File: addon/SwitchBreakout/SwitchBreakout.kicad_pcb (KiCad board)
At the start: 2 copper layers, 127.8 x 194.6 mm, 207 parts, among them IC1 SN74HCS72QPWRQ1, IC10 SN74HCS72QPWRQ1, IC11 SN74HCS72QPWRQ1, IC12 SN74HCS72QPWRQ1, IC13 SN74HCS72QPWRQ1, IC14 SN74HCS72QPWRQ1, IC15 SN74HCS72QPWRQ1, IC16 SN74HCS72QPWRQ1, IC2 SN74HCS72QPWRQ1, IC3 SN74HCS72QPWRQ1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

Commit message: Via whatever
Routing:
- net /C8: track 40.9 -> 205.5 mm, vias 0 -> 2
- net /C6: track 104.6 -> 214.5 mm, vias 0 -> 2
- net /C5: track 84.2 -> 188.3 mm, vias 0 -> 2
- net /C2: track 92.2 -> 171.2 mm, vias 0 -> 2
- net /C1: track 80.8 -> 159.6 mm, vias 0 -> 2
- net /C4: track 96.9 -> 175.3 mm, vias 0 -> 2
- net Net-(F11-Pad2): track 0.00 -> 4.93 mm
- net Net-(F15-Pad2): track 0.00 -> 4.93 mm
- net /D1: track 181.5 -> 184.0 mm
- net /D2: track 186.3 -> 188.1 mm
- net /D-Latch 1-8/BTN4: track 61.9 -> 62.5 mm

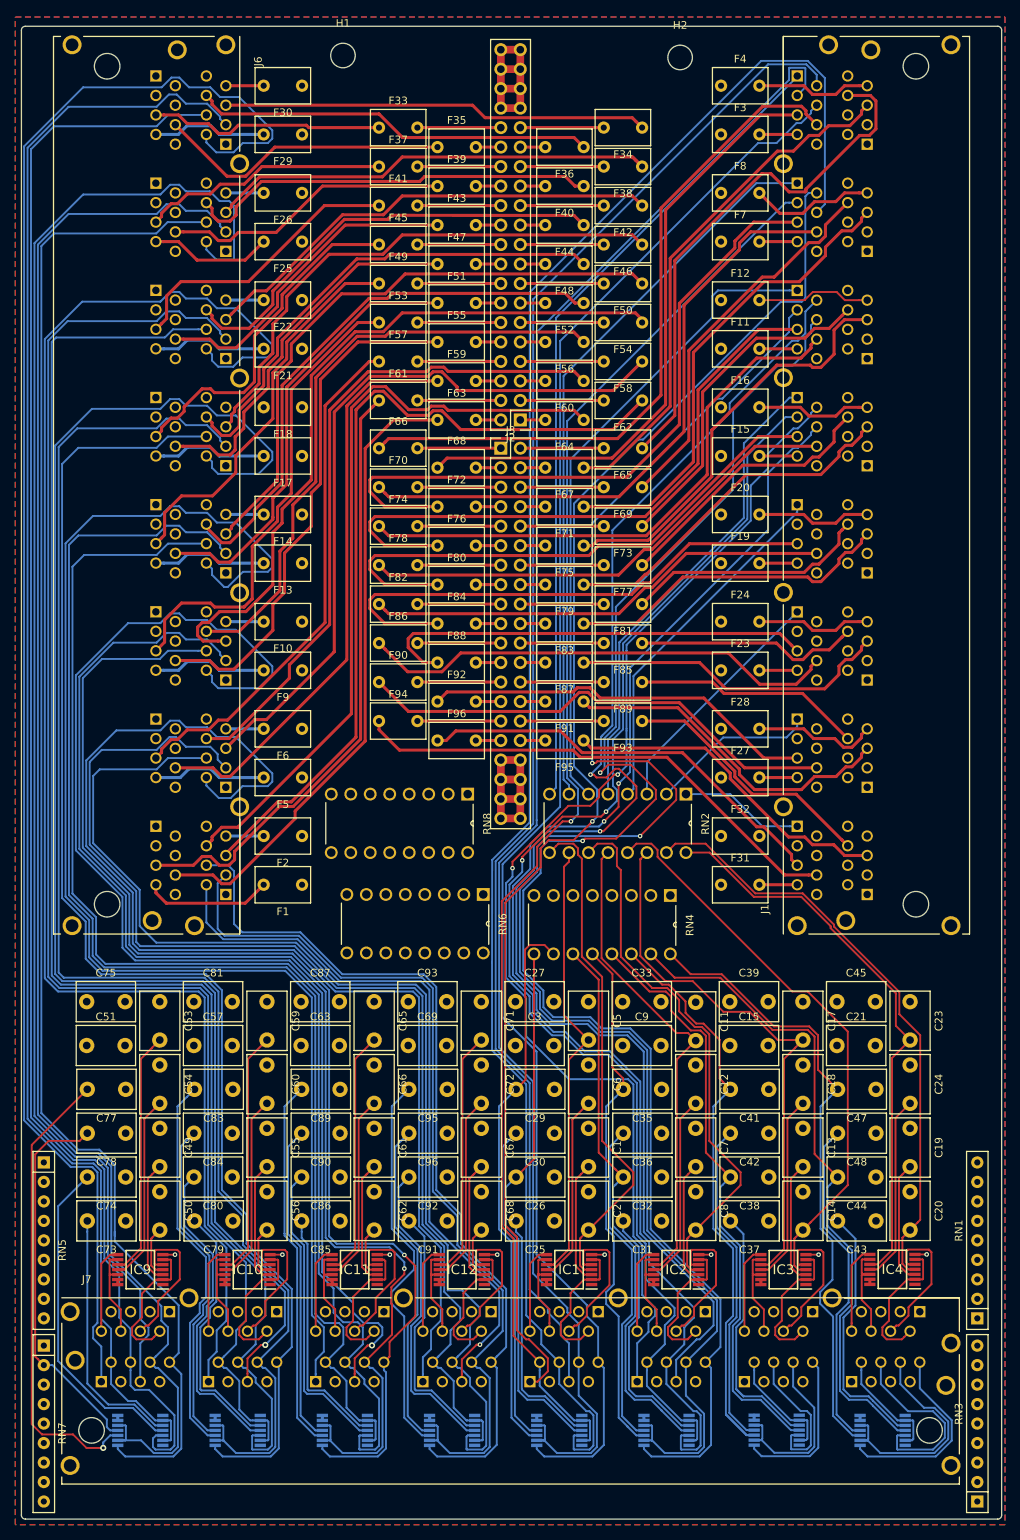
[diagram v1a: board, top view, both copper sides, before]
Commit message: Short stubs
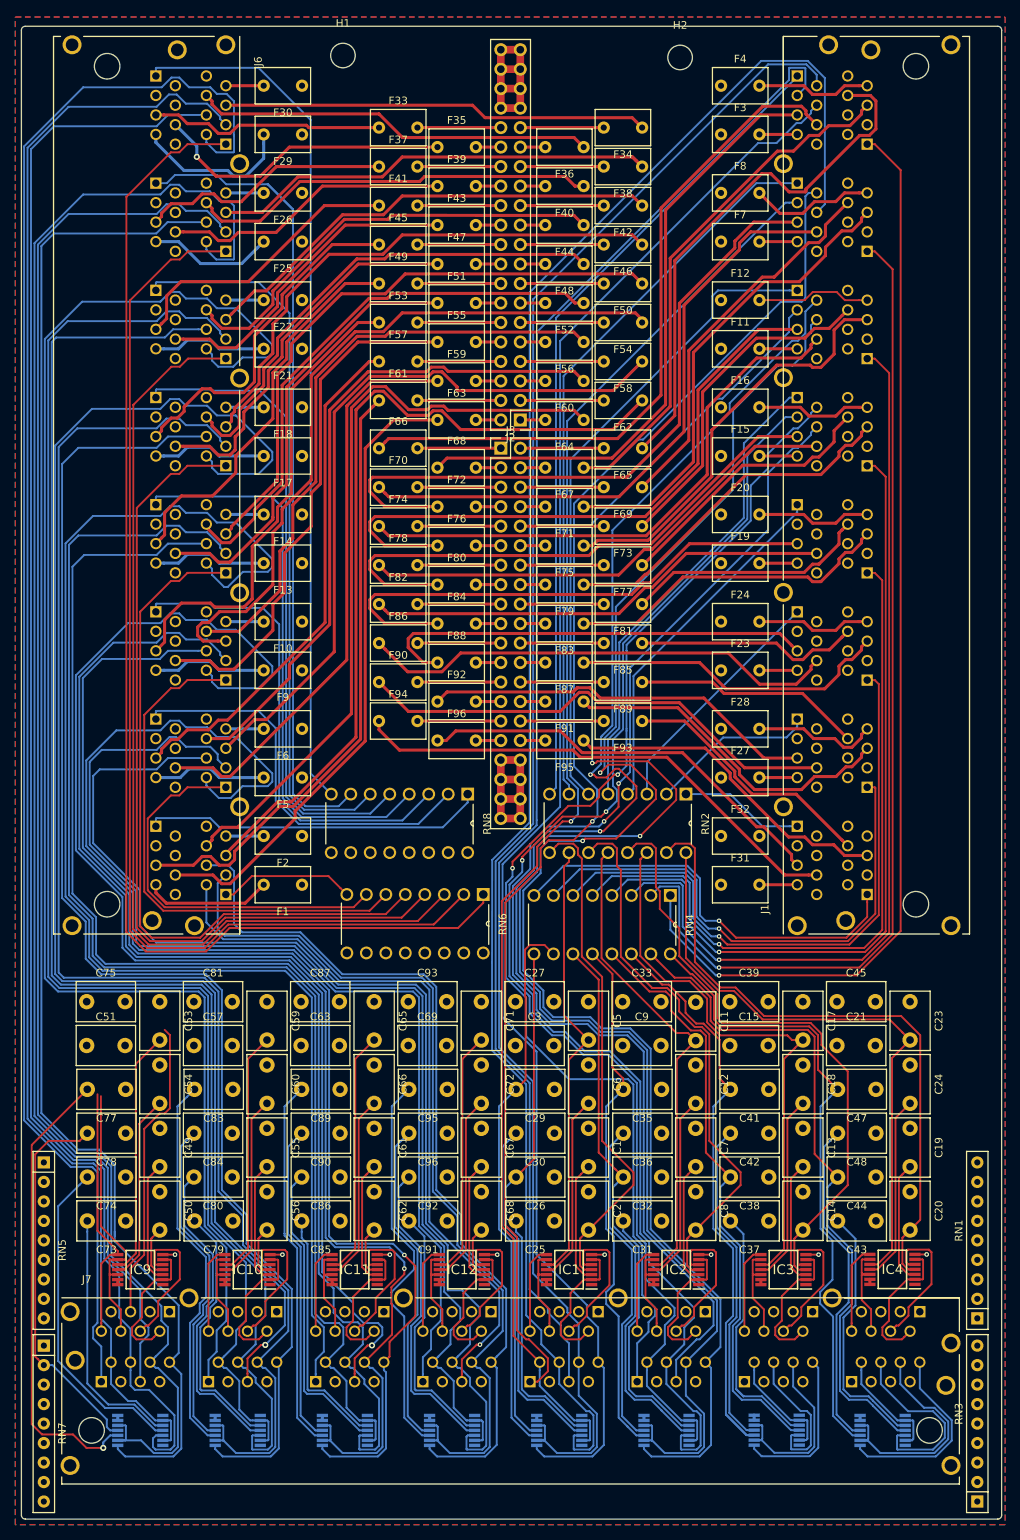
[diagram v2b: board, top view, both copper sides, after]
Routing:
- net /D-Latch 17-24/BTN8: track 0.00 -> 162.9 mm
- net /D-Latch 17-24/BTN7: track 0.00 -> 144.6 mm
- net /D-Lach 9-16/BTN8: track 0.00 -> 144.3 mm, vias 0 -> 1
- net /D-Lach 9-16/BTN7: track 0.00 -> 132.5 mm, vias 0 -> 1
- net /D-Latch 17-24/BTN6: track 0.00 -> 127.0 mm
- net /D-Lach 9-16/BTN6: track 0.00 -> 119.6 mm, vias 0 -> 1
- net /D-Latch 25-32/BTN1: track 0.00 -> 113.0 mm
- net /D-Latch 25-32/BTN2: track 0.00 -> 109.9 mm
- net /D-Latch 17-24/BTN5: track 0.00 -> 109.4 mm
- net /D-Lach 9-16/BTN5: track 0.00 -> 106.7 mm, vias 0 -> 1
- net /D-Latch 25-32/BTN3: track 0.00 -> 95.1 mm
- net /D-Lach 9-16/BTN4: track 0.00 -> 94.4 mm, vias 0 -> 1
- net /D-Latch 17-24/BTN4: track 0.00 -> 91.8 mm
- net /D-Latch 25-32/BTN4: track 0.00 -> 84.4 mm
- net /D-Lach 9-16/BTN3: track 0.00 -> 81.2 mm, vias 0 -> 1
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
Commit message: steps steps steps
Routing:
- net /M1: track 0.00 -> 220.2 mm
- net /M4: track 18.9 -> 236.3 mm, vias 0 -> 2
- net /M2: track 18.4 -> 235.0 mm
- net /M6: track 12.0 -> 210.9 mm, vias 0 -> 1
- net /D-Latch 17-24/D-Latch 0/BTN2: track 32.1 -> 109.2 mm
- net /D-Latch 25-32/D-Latch 0/BTN1: track 42.9 -> 105.2 mm, vias 0 -> 1
- net /D-Latch 17-24/D-Latch 0/BTN1: track 6.83 -> 68.6 mm
- net /D-Latch 25-32/D-Latch 1/BTN1: track 41.2 -> 101.3 mm, vias 0 -> 1
- net /D-Latch 17-24/D-Latch 1/BTN1: track 6.83 -> 62.5 mm
- net /D-Latch 25-32/D-Latch 2/BTN1: track 39.5 -> 92.4 mm, vias 0 -> 1
- net /D-Latch 25-32/D-Latch 0/BTN2: track 60.2 -> 108.9 mm, vias 1 -> 2
- net /D-Latch 25-32/D-Latch 4/BTN1: track 40.5 -> 86.9 mm, vias 0 -> 1
- net /D-Latch 25-32/D-Latch 1/BTN2: track 50.4 -> 96.5 mm, vias 0 -> 1
- net /D-Latch 17-24/D-Latch 2/BTN1: track 6.83 -> 52.2 mm
- net /P5: track 39.5 -> 0.00 mm
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
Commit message: bottom
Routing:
- net /D-Lach 9-16/D-Latch 0/CLK1: track 32.0 -> 95.7 mm, vias 0 -> 1
- net /D-Lach 9-16/D-Latch 0/CLK2: track 41.8 -> 105.0 mm, vias 0 -> 1
- net /D-Latch 25-32/D-Latch 4/CLK1: track 33.1 -> 92.0 mm, vias 0 -> 1
- net /D-Latch 25-32/D-Latch 4/CLK2: track 43.0 -> 96.0 mm, vias 0 -> 1
- net /D-Lach 9-16/D-Latch 1/CLK1: track 33.1 -> 81.9 mm, vias 0 -> 1
- net /D-Lach 9-16/D-Latch 1/CLK2: track 43.0 -> 90.9 mm, vias 0 -> 1
- net /D-Latch 25-32/D-Latch 2/CLK1: track 32.0 -> 76.1 mm, vias 0 -> 1
- net /D-Latch 25-32/D-Latch 2/CLK2: track 41.8 -> 79.8 mm, vias 0 -> 1
- net /D-Lach 9-16/D-Latch 2/CLK1: track 34.5 -> 67.1 mm, vias 0 -> 1
- net /D-Lach 9-16/D-Latch 2/CLK2: track 42.8 -> 74.9 mm, vias 0 -> 1
- net /D-Latch 25-32/D-Latch 1/CLK1: track 33.8 -> 62.7 mm, vias 0 -> 1
- net /D-Latch 25-32/D-Latch 1/CLK2: track 43.6 -> 65.9 mm, vias 0 -> 1
- net /D-Lach 9-16/D-Latch 4/CLK1: track 33.6 -> 55.3 mm, vias 0 -> 1
- net /D-Lach 9-16/D-Latch 4/CLK2: track 43.3 -> 64.9 mm, vias 0 -> 1
- net /D-Latch 25-32/D-Latch 0/CLK1: track 33.3 -> 43.9 mm, vias 0 -> 1
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
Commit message: details, details details
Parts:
- moved RN1 12.1 mm to (218.4, 170.2)
- moved RN5 11.6 mm to (102.9, 149.9)
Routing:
- net /H8: track 11.6 -> 205.5 mm
- net /H5: track 0.00 -> 189.0 mm
- net /H6: track 12.9 -> 199.7 mm
- net /H4: track 19.0 -> 189.7 mm
- net /H2: track 18.5 -> 181.1 mm
- net /H1: track 0.00 -> 161.2 mm
- net /B6: track 25.0 -> 172.0 mm
- net /G2: track 18.4 -> 165.2 mm, vias 0 -> 1
- net /B5: track 0.00 -> 146.8 mm
- net /G1: track 0.00 -> 145.1 mm, vias 0 -> 1
- net /D-Lach 9-16/BTN8: track 144.3 -> 0.00 mm, vias 1 -> 0
- net /B2: track 15.2 -> 157.7 mm
- net /D-Lach 9-16/BTN7: track 132.5 -> 0.00 mm, vias 1 -> 0
- net /B1: track 0.00 -> 128.7 mm
- net /D-Lach 9-16/BTN6: track 119.6 -> 0.00 mm, vias 1 -> 0
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
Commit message: More down
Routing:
- net /B8: track 21.2 -> 183.2 mm, vias 0 -> 2
- net /B4: track 19.0 -> 178.8 mm, vias 0 -> 1
- net /G6: track 12.0 -> 167.9 mm, vias 0 -> 1
- net /G5: track 0.00 -> 153.9 mm, vias 0 -> 1
- net /F5: track 0.00 -> 119.7 mm, vias 0 -> 1
- net /G8: track 11.4 -> 38.3 mm, vias 0 -> 1
- net /G1: track 145.1 -> 131.0 mm
- net /G2: track 165.2 -> 152.0 mm
- net /B2: track 157.7 -> 148.7 mm
- net /A8: track 132.6 -> 125.6 mm
- net /A6: track 139.5 -> 133.1 mm
- net /A1: track 102.3 -> 96.5 mm
- net /A5: track 114.0 -> 108.7 mm
- net /A4: track 118.2 -> 113.0 mm
- net /A2: track 112.0 -> 107.0 mm
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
